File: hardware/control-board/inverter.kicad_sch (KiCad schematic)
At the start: 0 parts

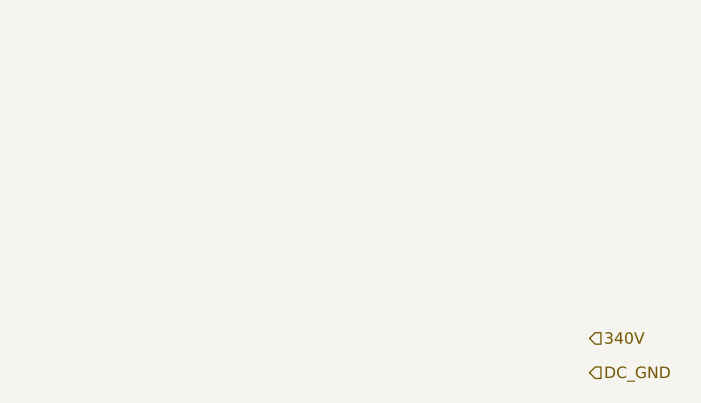
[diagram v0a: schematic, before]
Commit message: added basic LC series resonant tank
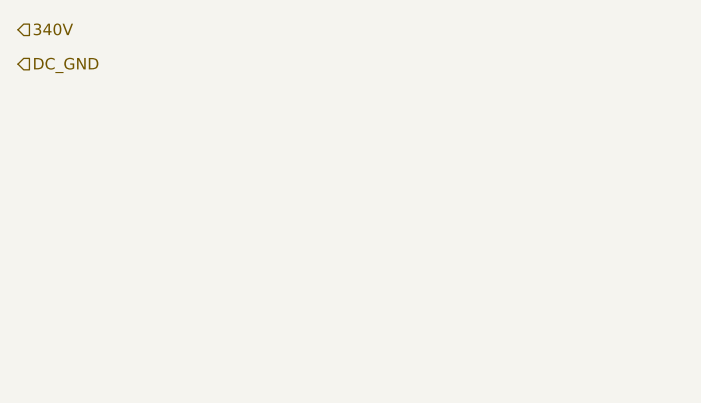
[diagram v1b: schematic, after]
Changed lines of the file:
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@@
 	(hierarchical_label "DC_GND"
 		(shape input)
-		(at 100.33 90.17 0)
+		(at 36.83 55.88 0)
 		(fields_autoplaced yes)
 		(effects
@@
 		)
 		(property "Netclass" "dc_bus_ground"
-			(at 100.33 91.44 0)
+			(at 36.83 57.15 0)
 			(effects
 				(font
@@
 	(hierarchical_label "340V"
 		(shape input)
-		(at 100.33 86.36 0)
+		(at 36.83 52.07 0)
 		(fields_autoplaced yes)
 		(effects
@@
 		)
 		(property "Netclass" "dc_bus_power"
-			(at 100.33 87.63 0)
+			(at 36.83 53.34 0)
 			(effects
 				(font

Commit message: added titles to sheets
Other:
- title: (none) -> Inverter
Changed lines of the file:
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@@
 	(generator_version "9.0")
 	(paper "A4")
+	(title_block
+		(title "Inverter")
+	)
 	(hierarchical_label "DC_GND"
 		(shape input)

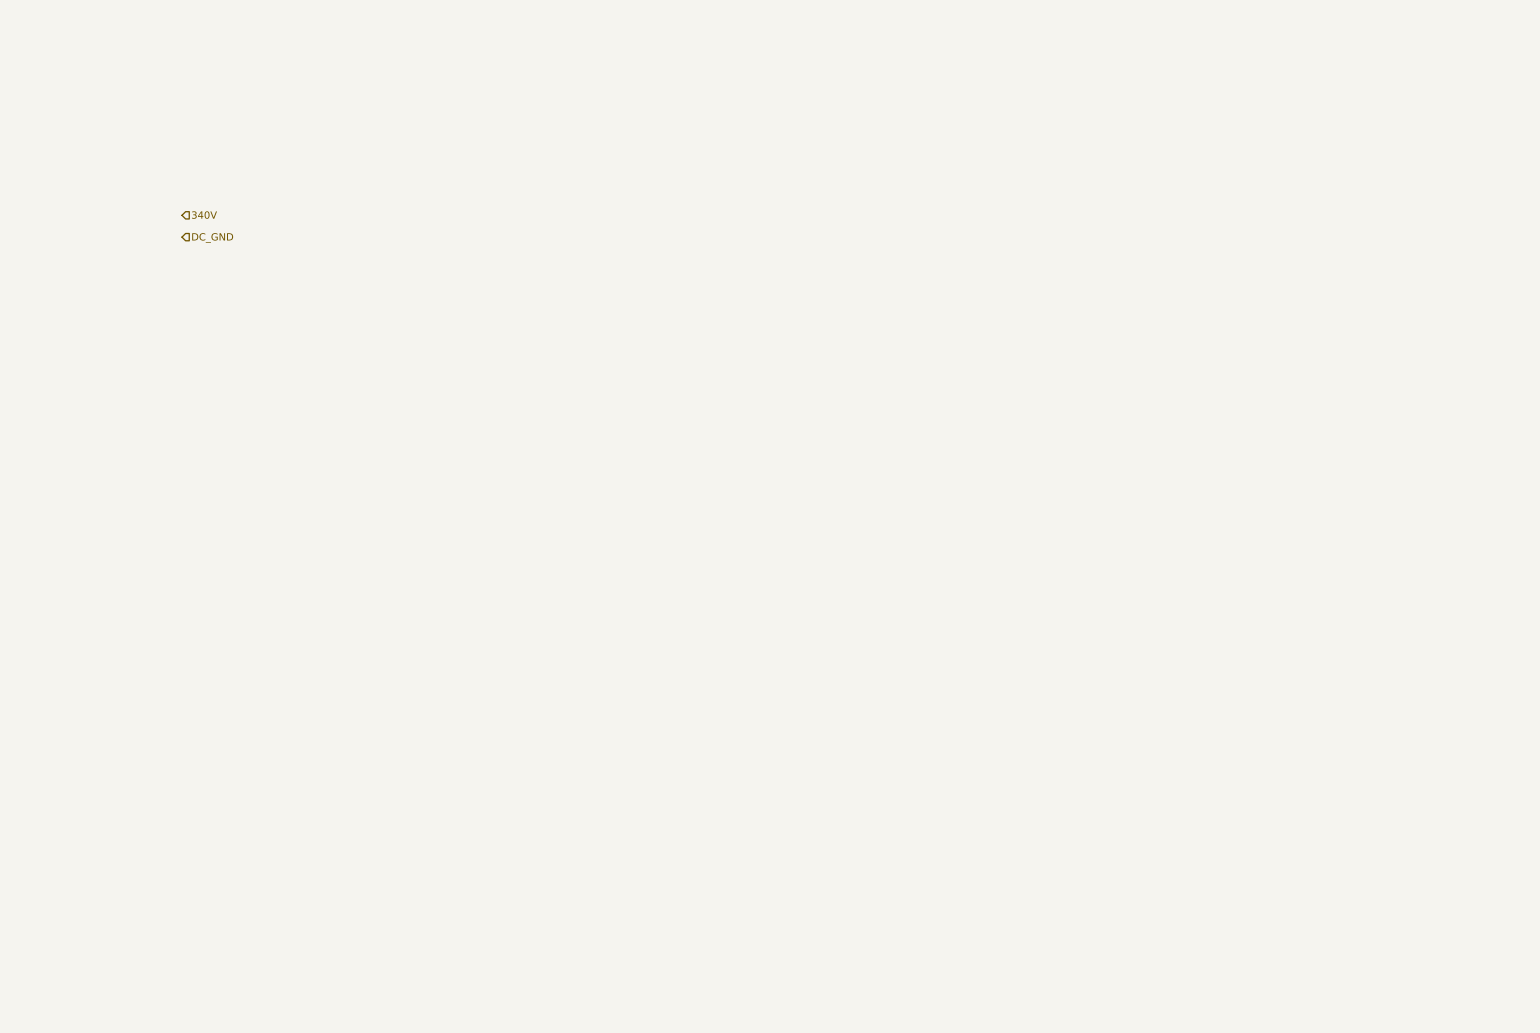
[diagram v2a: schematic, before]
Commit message: started work on inverter design
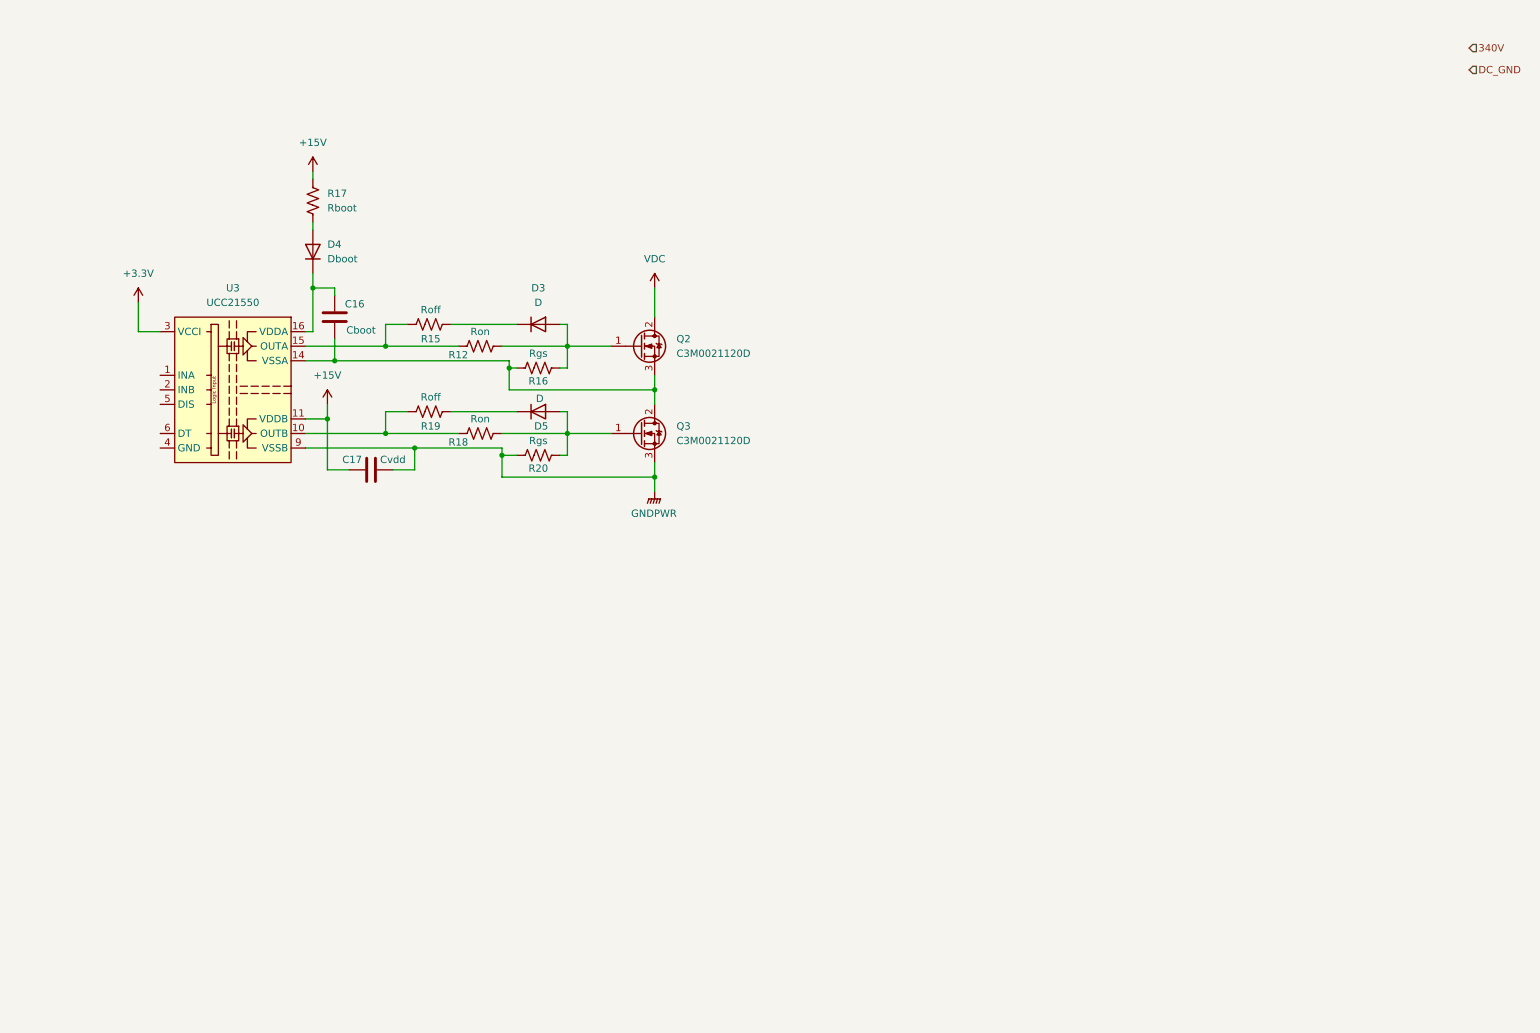
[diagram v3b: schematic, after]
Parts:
- added C16: Cboot, symbol Device:C
- added C17: Cvdd, symbol Device:C
- added D3, D5: D, symbol Device:D
- added D4: Dboot, symbol Device:D
- added Q2, Q3: C3M0021120D, Package_TO_SOT_THT:TO-247-3_Vertical, symbol sic_mosfet:C3M0021120D
- added R12, R18: Ron, symbol Device:R_US
- added R15, R19: Roff, symbol Device:R_US
- added R16, R20: Rgs, symbol Device:R_US
- added R17: Rboot, symbol Device:R_US
- added U3: UCC21550, Package_SO:SOIC-16W_7.5x10.3mm_P1.27mm, symbol gate_drivers:UCC21550
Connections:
- new net: R12.1, R15.1, U3.15 (OUTA)
- new net: D3.1 (K), R15.2
- new net: R18.1, R19.1, U3.10 (OUTB)
- new net: D5.2 (A), Q3.1 (G), R18.2, R20.2
- new net: C16.2, Q2.3 (S), Q3.2 (D), R16.1, U3.14 (VSSA)
- new net: D3.2 (A), Q2.1 (G), R12.2, R16.2
- new net: C16.1, D4.1 (K), U3.16 (VDDA)
- new net: D4.2 (A), R17.2
- new net: D5.1 (K), R19.2
- new net +15V: C17.2, R17.1, U3.11 (VDDB)
- new net +3.3V: U3.3 (VCCI), U3.8 (VCCI)
- new net GNDPWR: C17.1, Q3.3 (S), R20.1, U3.9 (VSSB)
- new net VDC: Q2.2 (D)

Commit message: reasearch, added section and finished negative bias addition to intervet side a
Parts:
- added C18: Cin, symbol Device:C
- added C19, C20: 33pF, symbol Device:C
- added C21: 1uF, symbol Device:C
- added C22, C23: C, symbol Device:C
- added D6, D7: D_Zener, symbol Device:D_Zener
- added R21, R22: 50, symbol Device:R_US
- added R23: 1k, symbol Device:R_US
- added R24: 50k, symbol Device:R_US
- C16: value Cboot -> 10uF
- C17: value Cvdd -> 1uF
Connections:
- net GNDPWR is gone; now on net DC_GND: C17.1, Q3.3 (S), R20.1, U3.9 (VSSB)
- net VDC is gone; now on net 340V: Q2.2 (D)
- net +15V: no longer R17.1
- net +3.3V: now also C21.1
- net 340V: now also C18.1
- net DC_GND: now also C18.2
- net at R12.1, R15.1: now also C22.2, D6.2 (A); no longer U3.15 (OUTA)
- net at R18.1, R19.1: now also C23.2, D7.2 (A); no longer U3.10 (OUTB)
- net TANK_A: now reaches C16.2, Q2.3 (S), Q3.2 (D), R16.1, U3.14 (VSSA)
- net at U3.1 (INA): now also C19.2, R21.2
- net at U3.2 (INB): now also C20.2, R22.2
- net GND: now reaches U3.4 (GND)
- net GND: now also C19.1, C20.1, C21.2, R23.1, R24.1
- net SIDE_A_DISABLE: now reaches U3.5 (DIS)
- net SIDE_A_DISABLE: now also R23.2
- net at U3.6 (DT): now also R24.2
- new net: C23.1, D7.1 (K), U3.10 (OUTB)
- new net: C22.1, D6.1 (K), U3.15 (OUTA)
- new net +24V: R17.1
- new net SIDE_A_INA: R21.1
- new net SIDE_A_INB: R22.1
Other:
- note added: "8.2.2.1"
- note added: "8.2.2.2"
- note added: "8.2.2.3"
- note added: "8.2.2.4"
- note added: "8.2.2.7.2"
- note added: "8.2.2.9 eg. 3"
- note added: "Bootstrap"
- note added: "Single supply full bridge Limitations: - must be run at 50%, the zener diode combined with the duty cycle determine the negative bias"
- moved on the sheet: C16, C17, D3, D4, D5, Q2, Q3, R12, R15, R16, R17, R18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

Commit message: selected 6V 5W zener diode for negative bias on gate driver
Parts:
- removed D6: D_Zener, symbol Device:D_Zener
- added D8: SMBJ5340B-TP, Diode_SMD:D_SMB, symbol Device:D_Zener
- D7: value D_Zener -> SMBJ5340B-TP; footprint (none) -> Diode_SMD:D_SMB
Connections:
- net at C22.2, R12.1, R15.1: now also D8.2 (A)
- net at C22.1, U3.15 (OUTA): now also D8.1 (K)
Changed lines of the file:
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@@
 			)
 		)
-		(property "Value" "D_Zener"
-			(at 156.718 73.152 0)
-			(effects
-				(font
-					(size 1.27 1.27)
-				)
-			)
-		)
-		(property "Footprint" ""
+		(property "Value" "SMBJ5340B-TP"
+			(at 160.528 73.406 0)
+			(effects
+				(font
+					(size 1.27 1.27)
+				)
+			)
+		)
+		(property "Footprint" "Diode_SMD:D_SMB"
 			(at 151.13 74.93 0)
 			(effects
@@
 			)
 		)
-		(property "Datasheet" "~"
+		(property "Datasheet" "https://www.mccsemi.com/pdf/Products/SMBJ5338B-SMBJ5388B(SMB).pdf"
 			(at 151.13 74.93 0)
 			(effects
@@
 			)
 		)
-		(property "Description" "Zener diode"
+		(property "Description" "6V 5W Zener Diode"
 			(at 151.13 74.93 0)
 			(effects
@@
 	)
 	(symbol
+		(lib_id "Device:D_Zener")
+		(at 151.13 59.69 0)
+		(unit 1)
+		(exclude_from_sim no)
+		(in_bom yes)
+		(on_board yes)
+		(dnp no)
+		(property "Reference" "D8"
+			(at 150.876 56.642 0)
+			(effects
+				(font
+					(size 1.27 1.27)
+				)
+			)
+		)
+		(property "Value" "SMBJ5340B-TP"
+			(at 160.528 58.166 0)
+			(effects
+				(font
+					(size 1.27 1.27)
+				)
+			)
+		)
+		(property "Footprint" "Diode_SMD:D_SMB"
+			(at 151.13 59.69 0)
+			(effects
+				(font
+					(size 1.27 1.27)
+				)
+				(hide yes)
+			)
+		)
+		(property "Datasheet" "https://www.mccsemi.com/pdf/Products/SMBJ5338B-SMBJ5388B(SMB).pdf"
+			(at 151.13 59.69 0)
+			(effects
+				(font
+					(size 1.27 1.27)
+				)
+				(hide yes)
+			)
+		)
+		(property "Description" "6V 5W Zener Diode"
+			(at 151.13 59.69 0)
+			(effects
+				(font
+					(size 1.27 1.27)
+				)
+				(hide yes)
+			)
+		)
+		(pin "1"
+		)
+		(pin "2"
+		)
+		(instances
+			(project "control-board"
+				(path "/19f0fb17-7370-4e5d-b0c6-f8a287a0a6cc/5e00e05d-479a-40b5-a7c4-ea384f0e6d47"
+					(reference "D8")
+					(unit 1)
+				)
+			)
+		)
+	)
+	(symbol
 		(lib_id "Device:C")
 		(at 85.09 54.61 0)
@@
 					(unit 1)
 				)
-			)
-		)
-	)
-	(symbol
-		(lib_id "Device:D_Zener")
-		(at 151.13 59.69 0)
-		(unit 1)
-		(exclude_from_sim no)
-		(in_bom yes)
-		(on_board yes)
-		(dnp no)
-		(property "Reference" "D6"
-			(at 150.876 56.642 0)
-			(effects
-				(font
-					(size 1.27 1.27)
-				)
-			)
-		)
-		(property "Value" "D_Zener"
-			(at 156.718 57.912 0)
-			(effects
-				(font
-					(size 1.27 1.27)
-				)
-			)
-		)
-		(property "Footprint" ""
-			(at 151.13 59.69 0)
-			(effects
-				(font
-					(size 1.27 1.27)
-				)
-				(hide yes)
-			)
-		)
-		(property "Datasheet" "~"
-			(at 151.13 59.69 0)
-			(effects
-				(font
-					(size 1.27 1.27)
-				)
-				(hide yes)
-			)
-		)
-		(property "Description" "Zener diode"
-			(at 151.13 59.69 0)
-			(effects
-				(font
-					(size 1.27 1.27)
-				)
-				(hide yes)
-			)
-		)
-		(pin "1"
-		)
-		(pin "2"
-		)
-		(instances
-			(project ""
-				(path "/19f0fb17-7370-4e5d-b0c6-f8a287a0a6cc/5e00e05d-479a-40b5-a7c4-ea384f0e6d47"
-					(reference "D6")
-					(unit 1)
-				)

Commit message: progress on component selection for inverter
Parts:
- C22, C23: value C -> 1uF
- D3, D5: value D -> MSS1P4-M3/89A; footprint (none) -> Diode_SMD:D_SMA
- D4: value Dboot -> C4D02120E; footprint (none) -> Package_TO_SOT_SMD:TO-252-2
- R12, R18: value Ron -> 3.3
- R17: value Rboot -> 2.6
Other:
- note added: "Dboot footprint might not be correct"
- note added: "Ron: (24.0 - 0.8) / ((1.47 * 5 * 3.3 * 3.3) / (1.47 + 5 + 3.3 + 3.3) -> 3.8A"
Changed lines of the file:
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@@
 		)
 	)
+	(text "Ron: (24.0 - 0.8) / ((1.47 * 5 * 3.3 * 3.3) / (1.47 + 5 + 3.3 + 3.3) -> 3.8A"
+		(exclude_from_sim no)
+		(at 88.138 181.356 0)
+		(effects
+			(font
+				(size 1.27 1.27)
+			)
+		)
+	)
 	(text "8.2.2.7.2"
 		(exclude_from_sim no)
@@
 	(text "8.2.2.9 eg. 3"
 		(exclude_from_sim no)
-		(at 162.306 50.292 0)
+		(at 162.814 50.8 0)
 		(effects
 			(font
@@
 		)
 	)
+	(text "Dboot footprint might not be correct"
+		(exclude_from_sim no)
+		(at 153.924 42.164 0)
+		(effects
+			(font
+				(size 1.27 1.27)
+			)
+		)
+	)
 	(text "8.2.2.1"
 		(exclude_from_sim no)
@@
 			)
 		)
-		(property "Value" "C"
-			(at 153.416 65.786 90)
+		(property "Value" "1uF"
+			(at 154.686 65.786 90)
 			(effects
 				(font
@@
 		(dnp no)
 		(property "Reference" "D7"
-			(at 150.876 71.882 0)
+			(at 147.32 73.66 0)
 			(effects
 				(font
@@
 		)
 		(property "Value" "SMBJ5340B-TP"
-			(at 160.528 73.406 0)
+			(at 160.782 76.454 0)
 			(effects
 				(font
@@
 			)
 		)
-		(property "Value" "Ron"
+		(property "Value" "3.3"
 			(at 187.96 72.39 90)
 			(effects
@@
 		)
 		(property "Value" "SMBJ5340B-TP"
-			(at 160.528 58.166 0)
+			(at 160.528 61.214 0)
 			(effects
 				(font
@@
 			)
 		)
-		(property "Value" "C"
-			(at 153.67 50.038 90)
+		(property "Value" "1uF"
+			(at 154.432 50.546 90)
 			(effects
 				(font
@@
 			)
 		)
-		(property "Value" "Dboot"
+		(property "Value" "C4D02120E"
 			(at 130.81 44.4499 90)
 			(effects
@@
 			)
 		)
-		(property "Footprint" ""
+		(property "Footprint" "Package_TO_SOT_SMD:TO-252-2"
 			(at 128.27 43.18 0)
 			(effects
@@
 			)
 		)
-		(property "Datasheet" "~"
+		(property "Datasheet" "https://assets.wolfspeed.com/uploads/2023/10/Wolfspeed_C4D02120E_data_sheet.pdf"
 			(at 128.27 43.18 0)
 			(effects
@@
 			)
 		)
-		(property "Value" "D"
+		(property "Value" "MSS1P4-M3/89A"
 			(at 198.12 52.07 0)
 			(effects
@@
 			)
 		)
-		(property "Footprint" ""
+		(property "Footprint" "Diode_SMD:D_SMA"
 			(at 198.12 55.88 0)
 			(effects
@@
 			)
 		)
-		(property "Datasheet" "~"
+		(property "Datasheet" "https://www.vishay.com/docs/89019/mss1p4.pdf"
 			(at 198.12 55.88 0)
 			(effects
@@
 			)
 		)
-		(property "Value" "Ron"
+		(property "Value" "3.3"
 			(at 187.96 57.15 90)
 			(effects
@@
 			)
 		)
-		(property "Value" "D"
+		(property "Value" "MSS1P4-M3/89A"
 			(at 198.374 68.834 0)
 			(effects
@@
 			)
 		)
-		(property "Footprint" ""
+		(property "Footprint" "Diode_SMD:D_SMA"
 			(at 198.12 71.12 0)
 			(effects
@@
 			)
 		)
-		(property "Datasheet" "~"
+		(property "Datasheet" "https://www.vishay.com/docs/89019/mss1p4.pdf"
 			(at 198.12 71.12 0)
 			(effects
@@
 			)
 		)
-		(property "Value" "Rboot"
+		(property "Value" "2.6"
 			(at 130.81 35.5599 0)
 			(effects

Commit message: finished single channel side a design
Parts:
- removed C18: Cin, symbol Device:C
- C16, C17: footprint (none) -> Capacitor_SMD:C_0805_2012Metric
- C19, C20, C21, C22, C23: footprint (none) -> Capacitor_SMD:C_0603_1608Metric
- R12, R15, R18, R19: footprint (none) -> Resistor_SMD:R_2512_6332Metric
- R16, R20, R21, R22, R23, R24: footprint (none) -> Resistor_SMD:R_0603_1608Metric
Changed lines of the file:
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@@
 	)
 	(junction
-		(at 218.44 52.07)
-		(diameter 0)
-		(color 0 0 0 0)
-	)
-	(junction
 		(at 171.45 74.93)
 		(diameter 0)
@@
 	(wire
 		(pts
-			(xy 218.44 52.07) (xy 218.44 54.61)
+			(xy 218.44 49.53) (xy 218.44 54.61)
 		)
 		(stroke
@@
 	(wire
 		(pts
-			(xy 238.76 82.55) (xy 218.44 82.55)
-		)
-		(stroke
-			(width 0)
-			(type default)
-		)
-	)
-	(wire
-		(pts
 			(xy 72.39 48.26) (xy 72.39 50.8)
 		)
@@
 	(wire
 		(pts
-			(xy 238.76 52.07) (xy 218.44 52.07)
-		)
-		(stroke
-			(width 0)
-			(type default)
-		)
-	)
-	(wire
-		(pts
 			(xy 154.94 67.31) (xy 162.56 67.31)
 		)
@@
 	(wire
 		(pts
-			(xy 238.76 71.12) (xy 238.76 82.55)
-		)
-		(stroke
-			(width 0)
-			(type default)
-		)
-	)
-	(wire
-		(pts
 			(xy 92.71 78.74) (xy 92.71 74.93)
 		)
@@
 	(wire
 		(pts
-			(xy 218.44 52.07) (xy 218.44 49.53)
-		)
-		(stroke
-			(width 0)
-			(type default)
-		)
-	)
-	(wire
-		(pts
 			(xy 140.97 82.55) (xy 144.78 82.55)
 		)
@@
 	(wire
 		(pts
-			(xy 238.76 52.07) (xy 238.76 63.5)
-		)
-		(stroke
-			(width 0)
-			(type default)
-		)
-	)
-	(wire
-		(pts
 			(xy 97.79 39.37) (xy 97.79 57.15)
 		)
@@
 			)
 		)
-		(property "Footprint" ""
+		(property "Footprint" "Resistor_SMD:R_0603_1608Metric"
 			(at 91.694 82.296 90)
 			(effects
@@
 			)
 		)
-		(property "Footprint" ""
+		(property "Footprint" "Resistor_SMD:R_2512_6332Metric"
 			(at 179.324 54.864 90)
 			(effects
@@
 			)
 		)
-		(property "Footprint" ""
+		(property "Footprint" "Capacitor_SMD:C_0603_1608Metric"
 			(at 73.3552 58.42 0)
 			(effects
@@
 			)
 		)
-		(property "Footprint" ""
+		(property "Footprint" "Capacitor_SMD:C_0603_1608Metric"
 			(at 154.94 66.3448 0)
 			(effects
@@
 			)
 		)
-		(property "Footprint" ""
+		(property "Footprint" "Resistor_SMD:R_2512_6332Metric"
 			(at 188.214 73.914 90)
 			(effects
@@
 			)
 		)
-		(property "Footprint" ""
+		(property "Footprint" "Capacitor_SMD:C_0603_1608Metric"
 			(at 86.0552 58.42 0)
 			(effects
@@
 			)
 		)
-		(property "Footprint" ""
+		(property "Footprint" "Capacitor_SMD:C_0603_1608Metric"
 			(at 107.95 38.4048 0)
 			(effects
@@
 			)
 		)
-		(property "Footprint" ""
+		(property "Footprint" "Capacitor_SMD:C_0603_1608Metric"
 			(at 154.94 51.1048 0)
 			(effects
@@
 	)
 	(symbol
-		(lib_id "Device:C")
-		(at 238.76 67.31 0)
-		(unit 1)
-		(exclude_from_sim no)
-		(in_bom yes)
-		(on_board yes)
-		(dnp no)
-		(fields_autoplaced yes)
-		(property "Reference" "C18"
-			(at 242.57 66.0399 0)
-			(effects
-				(font
-					(size 1.27 1.27)
-				)
-				(justify left)
-			)
-		)
-		(property "Value" "Cin"
-			(at 242.57 68.5799 0)
-			(effects
-				(font
-					(size 1.27 1.27)
-				)
-				(justify left)
-			)
-		)
-		(property "Footprint" ""
-			(at 239.7252 71.12 0)
-			(effects
-				(font
-					(size 1.27 1.27)
-				)
-				(hide yes)
-			)
-		)
-		(property "Datasheet" "~"
-			(at 238.76 67.31 0)
-			(effects
-				(font
-					(size 1.27 1.27)
-				)
-				(hide yes)
-			)
-		)
-		(property "Description" "Unpolarized capacitor"
-			(at 238.76 67.31 0)
-			(effects
-				(font
-					(size 1.27 1.27)
-				)
-				(hide yes)
-			)
-		)
-		(pin "1"
-		)
-		(pin "2"
-		)
-		(instances
-			(project ""
-				(path "/19f0fb17-7370-4e5d-b0c6-f8a287a0a6cc/5e00e05d-479a-40b5-a7c4-ea384f0e6d47"
-					(reference "C18")
-					(unit 1)
-				)
-			)
-		)
-	)
-	(symbol
 		(lib_id "power:GND")
 		(at 92.71 88.9 0)
@@
 			)
 		)
-		(property "Footprint" ""
+		(property "Footprint" "Resistor_SMD:R_0603_1608Metric"
 			(at 198.374 62.484 90)
 			(effects
@@
 			)
 		)
-		(property "Footprint" ""
+		(property "Footprint" "Resistor_SMD:R_2512_6332Metric"
 			(at 188.214 58.674 90)
 			(effects
@@
 			)
 		)
-		(property "Footprint" ""
+		(property "Footprint" "Resistor_SMD:R_0603_1608Metric"
 			(at 84.074 75.946 90)
 			(effects
@@
 			)
 		)
-		(property "Footprint" ""
+		(property "Footprint" "Capacitor_SMD:C_0805_2012Metric"
 			(at 133.0452 58.42 0)
 			(effects
@@
 			)
 		)
-		(property "Footprint" ""
+		(property "Footprint" "Resistor_SMD:R_0603_1608Metric"
 			(at 198.374 77.724 90)
 			(effects
@@
 			)
 		)
-		(property "Footprint" ""
+		(property "Footprint" "Resistor_SMD:R_0603_1608Metric"
 			(at 66.294 63.754 90)
 			(effects
@@
 			)
 		)
-		(property "Footprint" ""
+		(property "Footprint" "Resistor_SMD:R_0603_1608Metric"
 			(at 77.724 66.294 90)
 			(effects
@@
 			)
 		)
-		(property "Footprint" ""
+		(property "Footprint" "Capacitor_SMD:C_0805_2012Metric"
 			(at 133.35 83.5152 0)
 			(effects
@@
 			)
 		)
-		(property "Footprint" ""
+		(property "Footprint" "Resistor_SMD:R_2512_6332Metric"
 			(at 179.324 70.104 90)
 			(effects
